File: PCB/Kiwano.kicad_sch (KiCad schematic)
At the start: 50 parts, among them J1 VIK Module, J2 Cirque, J3 RGB_EX, SW1 PER56, U1 PMW3360DM-T2QU, U2 AP2127K-ADJ

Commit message: 30/07/2023 update
Updated BOM.
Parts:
- D1, D2, D3, D4, D5, D6, D7, D8: LCSC C5242955 -> C524051
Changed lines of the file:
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@@
       (effects (font (size 1.27 1.27)) hide)
     )
-    (property "LCSC" "C5242955" (at 33.02 139.7 0)
+    (property "LCSC" "C524051" (at 33.02 139.7 0)
       (effects (font (size 1.27 1.27)) hide)
     )
@@
       (effects (font (size 1.27 1.27)) hide)
     )
-    (property "LCSC" "C5242955" (at 139.7 139.7 0)
+    (property "LCSC" "C524051" (at 139.7 139.7 0)
       (effects (font (size 1.27 1.27)) hide)
     )
@@
       (effects (font (size 1.27 1.27)) hide)
     )
-    (property "LCSC" "C5242955" (at 121.92 139.7 0)
+    (property "LCSC" "C524051" (at 121.92 139.7 0)
       (effects (font (size 1.27 1.27)) hide)
     )
@@
       (effects (font (size 1.27 1.27)) hide)
     )
-    (property "LCSC" "C5242955" (at 68.58 139.7 0)
+    (property "LCSC" "C524051" (at 68.58 139.7 0)
       (effects (font (size 1.27 1.27)) hide)
     )
@@
       (effects (font (size 1.27 1.27)) hide)
     )
-    (property "LCSC" "C5242955" (at 86.36 139.7 0)
+    (property "LCSC" "C524051" (at 86.36 139.7 0)
       (effects (font (size 1.27 1.27)) hide)
     )
@@
       (effects (font (size 1.27 1.27)) hide)
     )
-    (property "LCSC" "C5242955" (at 50.8 139.7 0)
+    (property "LCSC" "C524051" (at 50.8 139.7 0)
       (effects (font (size 1.27 1.27)) hide)
     )
@@
       (effects (font (size 1.27 1.27)) hide)
     )
-    (property "LCSC" "C5242955" (at 157.48 139.7 0)
+    (property "LCSC" "C524051" (at 157.48 139.7 0)
       (effects (font (size 1.27 1.27)) hide)
     )
@@
       (effects (font (size 1.27 1.27)) hide)
     )
-    (property "LCSC" "C5242955" (at 104.14 139.7 0)
-      (effects (font (size 1.27 1.27)) hide)
-    )
+    (property "LCSC" "C524051" (at 104.14 139.7 0)
+      (effects (font (size 1.27 1.27)) hide)
+    )

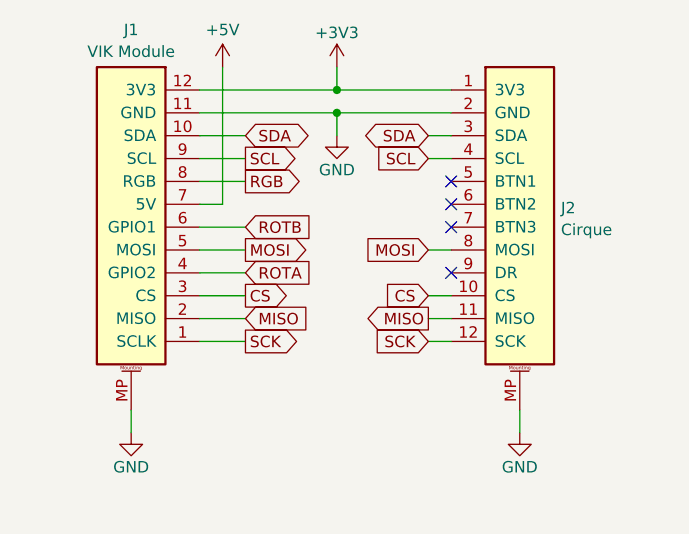
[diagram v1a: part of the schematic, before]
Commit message: 04/08/2023 update
Updated SK6812 MINI-E and switch footprints. Changed VIK FFC to FH12. Stitched ground planes together. Fixed VIK footprint. Moved production files to easier to access location.
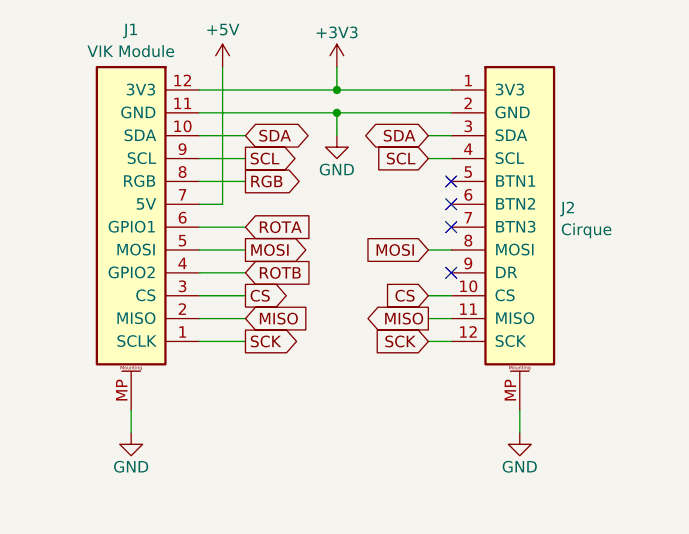
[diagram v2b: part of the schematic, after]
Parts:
- J1, J2: LCSC C424659 -> C88360
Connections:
- net ROTA: now also J1.6 (GPIO1); no longer J1.4 (GPIO2)
- net ROTB: now also J1.4 (GPIO2); no longer J1.6 (GPIO1)
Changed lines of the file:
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@@
     )
   )
-  (global_label "ROTB" (shape input) (at 40.64 43.18 0) (fields_autoplaced)
-    (effects (font (size 1.27 1.27)) (justify left))
-    (property "Intersheetrefs" "${INTERSHEET_REFS}" (at 48.4633 43.18 0)
-      (effects (font (size 1.27 1.27)) (justify left) hide)
-    )
-  )
-  (global_label "ROTA" (shape input) (at 40.64 48.26 0) (fields_autoplaced)
-    (effects (font (size 1.27 1.27)) (justify left))
-    (property "Intersheetrefs" "${INTERSHEET_REFS}" (at 48.2819 48.26 0)
+  (global_label "ROTB" (shape input) (at 40.64 48.26 0) (fields_autoplaced)
+    (effects (font (size 1.27 1.27)) (justify left))
+    (property "Intersheetrefs" "${INTERSHEET_REFS}" (at 48.4633 48.26 0)
+      (effects (font (size 1.27 1.27)) (justify left) hide)
+    )
+  )
+  (global_label "ROTA" (shape input) (at 40.64 43.18 0) (fields_autoplaced)
+    (effects (font (size 1.27 1.27)) (justify left))
+    (property "Intersheetrefs" "${INTERSHEET_REFS}" (at 48.2819 43.18 0)
       (effects (font (size 1.27 1.27)) (justify left) hide)
     )
@@
       (effects (font (size 1.27 1.27)) hide)
     )
-    (property "LCSC" "C424659" (at 27.94 40.64 0)
+    (property "LCSC" "C88360" (at 27.94 40.64 0)
       (effects (font (size 1.27 1.27)) hide)
     )
@@
       (effects (font (size 1.27 1.27)) hide)
     )
-    (property "LCSC" "C424659" (at 71.12 40.64 0)
-      (effects (font (size 1.27 1.27)) hide)
-    )
+    (property "LCSC" "C88360" (at 71.12 40.64 0)
+      (effects (font (size 1.27 1.27)) hide)
+    )

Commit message: 28/08/2023 update
Unified component libraries into one big library. Fixed 3DP files.
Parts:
- A1: footprint Kiwano:Ariamelon_Logo_Mask -> Ariamelon-Logo:Ariamelon_Logo_Small_Mask
- A2: footprint Kiwano:vik-logo-small -> Ariamelon-Logo:VIK_Logo_Small
- D1, D2, D3, D4, D5, D6, D7, D8: footprint Kiwano:YS-SK6812MINI-E -> Ariamelon-Device:LED_OPSCO_SK6812MINI-E; symbol Honeydew:SK6812MINI-E -> Ariamelon-Device:SK6812MINI-E
- H1, H2, H3: footprint Kiwano:JLC Tooling Hole -> Ariamelon-HolePad:MountingHole_JLC-Tooling
- H4, H5, H6, H7, H8, H9: footprint Kiwano:MountingHole_3.2mm_M3_Pad -> Ariamelon-HolePad:MountingHole_3.2mm_M3_Pad
- J1: footprint Kiwano:vik-module-connector-horizontal -> Ariamelon-Connector:VIK_Module_Horizontal; symbol Crenshaw:vik-module-connector -> Ariamelon-Connector:VIK Module Connector
- J2: value Cirque -> VIK Cirque Connector; footprint Kiwano:vik-cirque-connector-horizontal -> Ariamelon-Connector:VIK_Cirque_Horizontal; symbol Kiwano:Cirque -> Ariamelon-Connector:VIK Cirque Connector
- J3: footprint Kiwano:Header_RGB -> Ariamelon-Header:PinHeader_RGB
- SW1: footprint Kiwano:PER56 -> Ariamelon-RotaryEncoder:RotaryEncoder_Bourns_PER561-P115-N0015
- U1: value PMW3360DM-T2QU -> PMW3360DM-T2QU_1; footprint Kiwano:IC_PMW3360DM-T2QU -> Ariamelon-Package:PixArt_PMW3360DM-T2QU; symbol Ogen:PMW3360DM-T2QU -> Ariamelon-IC:PMW3360DM-T2QU_1

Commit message: V1.1 update
Changed LDO to XC6206P202MR. Removed RC filter and pullup from encoder pins.
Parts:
- removed C13, C14: 10n, Capacitor_SMD:C_0402_1005Metric, symbol Device:C_Small
- removed R4, R6, R7, R8, R9: 10k, Resistor_SMD:R_0402_1005Metric, symbol Device:R_Small
- removed R5: 15k, Resistor_SMD:R_0402_1005Metric, symbol Device:R_Small
- removed U2: AP2127K-ADJ, Package_TO_SOT_SMD:SOT-23-5, symbol Regulator_Linear:AP2127K-ADJ
- added U2: XC6206P202MR, Ariamelon-Package:SOT-23-3, symbol Regulator_Linear:XC6206PxxxMR
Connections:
- net +2V: now also U2.2 (VO)
- net +3V3: now also U2.3 (VI)
- net GND: now also U2.1 (GND)
- net ROTA: now also SW1.A
- net ROTB: now also SW1.B
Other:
- moved on the sheet: C11, C12
